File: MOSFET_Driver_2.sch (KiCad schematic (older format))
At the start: 20 parts, among them Q10 TPHR8504PL, Q11 TPHR8504PL, Q12 TPHR8504PL, Q7 TPHR8504PL, Q8 TPHR8504PL, Q9 TPHR8504PL, U1 FD6288Q

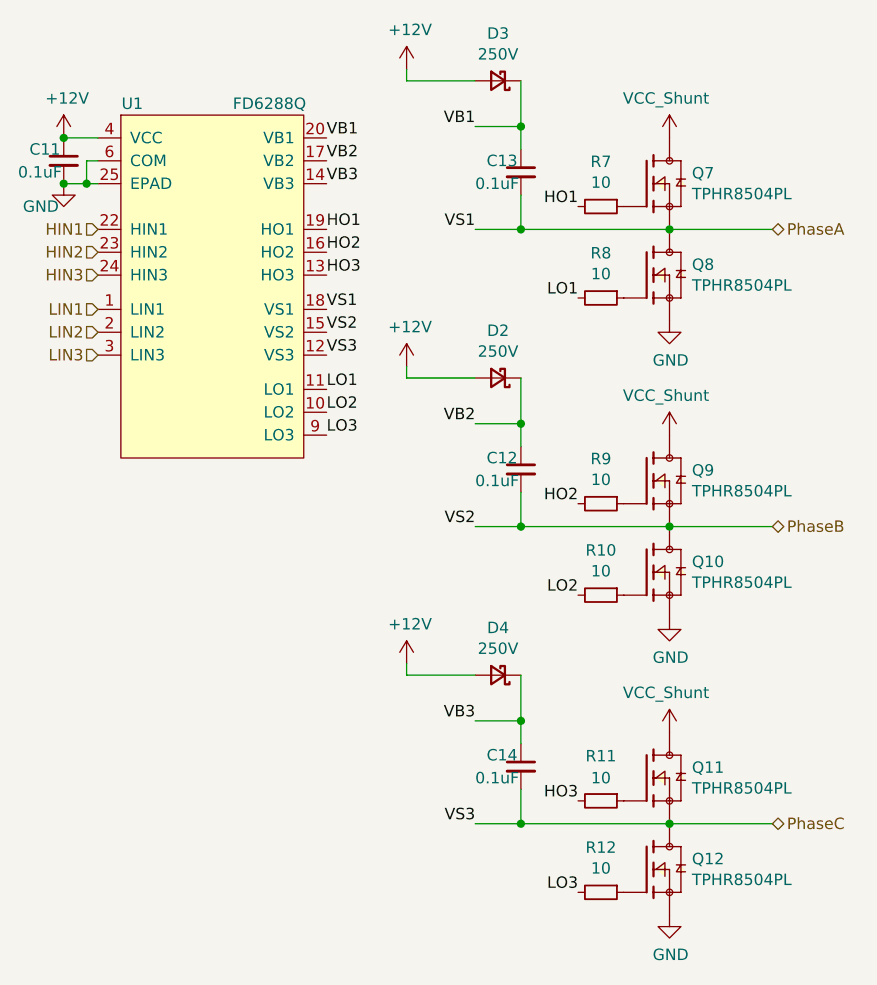
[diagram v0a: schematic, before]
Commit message: Added the rest of the phases and their associated components
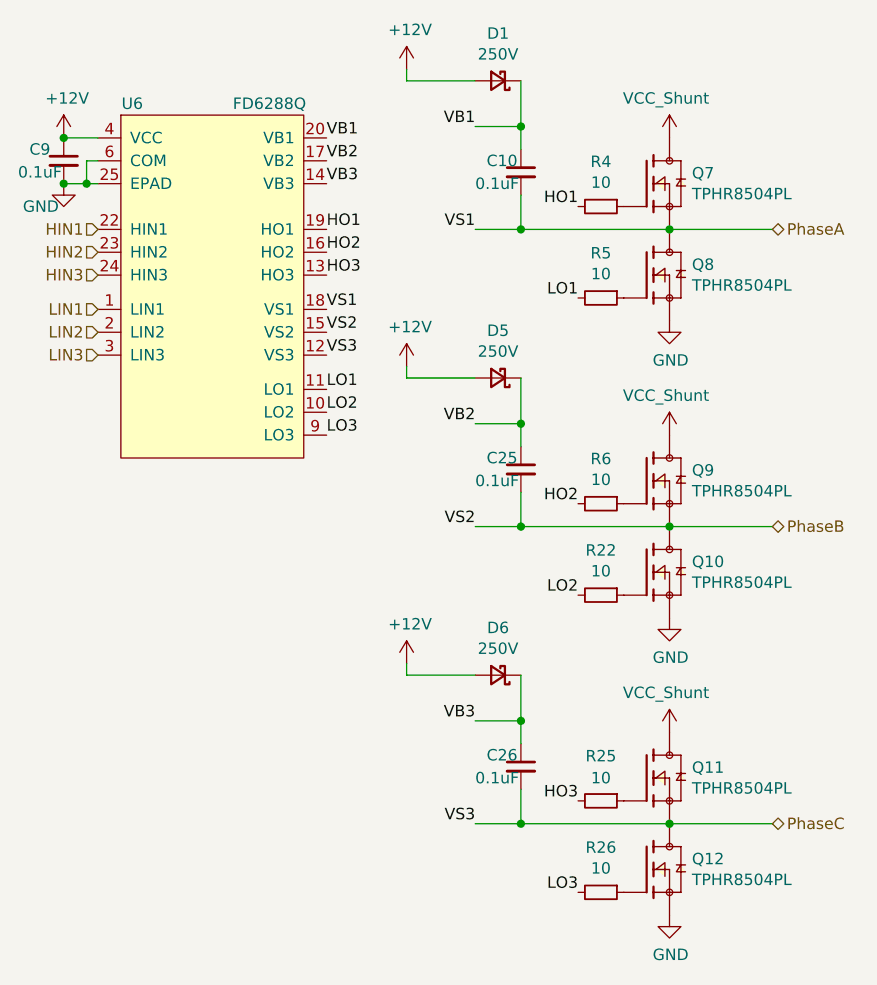
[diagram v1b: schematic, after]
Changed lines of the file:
@@
 $Descr A4 11693 8268
 encoding utf-8
-Sheet 6 7
+Sheet 7 11
 Title ""
 Date ""
@@
 AR Path="/605793F0/603754E4" Ref="U6"  Part="1"
 AR Path="/6057AB51/603754E4" Ref="U?"  Part="1"
-F 0 "U?" H 5800 1650 50  0000 C CNN
+F 0 "U6" H 5800 1650 50  0000 C CNN
 F 1 "FD6288Q" H 6400 1650 50  0000 C CNN
 F 2 "Package_DFN_QFN:QFN-24-1EP_4x4mm_P0.5mm_EP2.7x2.7mm" H 6175 2000 50  0001 C CNN
@@
 AR Path="/605793F0/6057ED5C" Ref="#PWR0136"  Part="1"
 AR Path="/6057AB51/6057ED5C" Ref="#PWR?"  Part="1"
-F 0 "#PWR?" H 5500 1950 50  0001 C CNN
+F 0 "#PWR0136" H 5500 1950 50  0001 C CNN
 F 1 "GND" H 5400 2100 50  0000 C CNN
 F 2 "" H 5500 2200 50  0001 C CNN
@@
 AR Path="/605793F0/6057ED5D" Ref="C9"  Part="1"
 AR Path="/6057AB51/6057ED5D" Ref="C?"  Part="1"
-F 0 "C?" H 5350 2150 50  0000 L CNN
+F 0 "C9" H 5350 2150 50  0000 L CNN
 F 1 "0.1uF" H 5300 2050 50  0000 L CNN
 F 2 "Capacitor_SMD:C_0402_1005Metric" H 5500 2100 50  0001 C CNN
@@
 AR Path="/605793F0/6057ED6E" Ref="#PWR0137"  Part="1"
 AR Path="/6057AB51/6057ED6E" Ref="#PWR?"  Part="1"
-F 0 "#PWR?" H 8150 2550 50  0001 C CNN
+F 0 "#PWR0137" H 8150 2550 50  0001 C CNN
 F 1 "GND" H 8155 2627 50  0000 C CNN
 F 2 "" H 8150 2800 50  0001 C CNN
@@
 AR Path="/605793F0/6057B9E1" Ref="R5"  Part="1"
 AR Path="/6057AB51/6057B9E1" Ref="R?"  Part="1"
-F 0 "R?" V 7654 2700 50  0000 C CNN
+F 0 "R5" V 7654 2700 50  0000 C CNN
 F 1 "10" V 7745 2700 50  0000 C CNN
 F 2 "Resistor_SMD:R_0402_1005Metric" H 7850 2700 50  0001 C CNN
@@
 AR Path="/605793F0/6057B9E2" Ref="R4"  Part="1"
 AR Path="/6057AB51/6057B9E2" Ref="R?"  Part="1"
-F 0 "R?" V 7654 2300 50  0000 C CNN
+F 0 "R4" V 7654 2300 50  0000 C CNN
 F 1 "10" V 7745 2300 50  0000 C CNN
 F 2 "Resistor_SMD:R_0402_1005Metric" H 7850 2300 50  0001 C CNN
@@
 AR Path="/605793F0/6057B9E3" Ref="#PWR0138"  Part="1"
 AR Path="/6057AB51/6057B9E3" Ref="#PWR?"  Part="1"
-F 0 "#PWR?" H 8150 3850 50  0001 C CNN
+F 0 "#PWR0138" H 8150 3850 50  0001 C CNN
 F 1 "GND" H 8155 3927 50  0000 C CNN
 F 2 "" H 8150 4100 50  0001 C CNN
@@
 AR Path="/605793F0/6057B9E4" Ref="R22"  Part="1"
 AR Path="/6057AB51/6057B9E4" Ref="R?"  Part="1"
-F 0 "R?" V 7654 4000 50  0000 C CNN
+F 0 "R22" V 7654 4000 50  0000 C CNN
 F 1 "10" V 7745 4000 50  0000 C CNN
 F 2 "Resistor_SMD:R_0402_1005Metric" H 7850 4000 50  0001 C CNN
@@
 AR Path="/605793F0/6057B9E5" Ref="R6"  Part="1"
 AR Path="/6057AB51/6057B9E5" Ref="R?"  Part="1"
-F 0 "R?" V 7654 3600 50  0000 C CNN
+F 0 "R6" V 7654 3600 50  0000 C CNN
 F 1 "10" V 7745 3600 50  0000 C CNN
 F 2 "Resistor_SMD:R_0402_1005Metric" H 7850 3600 50  0001 C CNN
@@
 AR Path="/605793F0/6057ED61" Ref="#PWR0139"  Part="1"
 AR Path="/6057AB51/6057ED61" Ref="#PWR?"  Part="1"
-F 0 "#PWR?" H 8150 5150 50  0001 C CNN
+F 0 "#PWR0139" H 8150 5150 50  0001 C CNN
 F 1 "GND" H 8155 5227 50  0000 C CNN
 F 2 "" H 8150 5400 50  0001 C CNN
@@
 AR Path="/605793F0/6057ED62" Ref="R26"  Part="1"
 AR Path="/6057AB51/6057ED62" Ref="R?"  Part="1"
-F 0 "R?" V 7654 5300 50  0000 C CNN
+F 0 "R26" V 7654 5300 50  0000 C CNN
 F 1 "10" V 7745 5300 50  0000 C CNN
 F 2 "Resistor_SMD:R_0402_1005Metric" H 7850 5300 50  0001 C CNN
@@
 AR Path="/605793F0/6057ED5E" Ref="D5"  Part="1"
 AR Path="/6057AB51/6057ED5E" Ref="D?"  Part="1"
-F 0 "D?" H 7400 2843 50  0000 C CNN
+F 0 "D5" H 7400 2843 50  0000 C CNN
 F 1 "250V" H 7400 2934 50  0000 C CNN
 F 2 "Diode_SMD:D_SOD-523" V 7400 3050 50  0001 C CNN
@@
 AR Path="/605793F0/6057ED5F" Ref="C25"  Part="1"
 AR Path="/6057AB51/6057ED5F" Ref="C?"  Part="1"
-F 0 "C?" H 7350 3500 50  0000 L CNN
+F 0 "C25" H 7350 3500 50  0000 L CNN
 F 1 "0.1uF" H 7300 3400 50  0000 L CNN
 F 2 "Capacitor_SMD:C_0603_1608Metric" H 7500 3450 50  0001 C CNN
@@
 AR Path="/605793F0/6057ED6F" Ref="D1"  Part="1"
 AR Path="/6057AB51/6057ED6F" Ref="D?"  Part="1"
-F 0 "D?" H 7400 1543 50  0000 C CNN
+F 0 "D1" H 7400 1543 50  0000 C CNN
 F 1 "250V" H 7400 1634 50  0000 C CNN
 F 2 "Diode_SMD:D_SOD-523" V 7400 1750 50  0001 C CNN
@@
 AR Path="/605793F0/6057ED60" Ref="C10"  Part="1"
 AR Path="/6057AB51/6057ED60" Ref="C?"  Part="1"
-F 0 "C?" H 7350 2200 50  0000 L CNN
+F 0 "C10" H 7350 2200 50  0000 L CNN
 F 1 "0.1uF" H 7300 2100 50  0000 L CNN
 F 2 "Capacitor_SMD:C_0603_1608Metric" H 7500 2150 50  0001 C CNN
@@
 AR Path="/605793F0/6057B9DF" Ref="D6"  Part="1"
 AR Path="/6057AB51/6057B9DF" Ref="D?"  Part="1"
-F 0 "D?" H 7400 4143 50  0000 C CNN
+F 0 "D6" H 7400 4143 50  0000 C CNN
 F 1 "250V" H 7400 4234 50  0000 C CNN
 F 2 "Diode_SMD:D_SOD-523" V 7400 4350 50  0001 C CNN
@@
 AR Path="/605793F0/6057ED71" Ref="C26"  Part="1"
 AR Path="/6057AB51/6057ED71" Ref="C?"  Part="1"
-F 0 "C?" H 7350 4800 50  0000 L CNN
+F 0 "C26" H 7350 4800 50  0000 L CNN
 F 1 "0.1uF" H 7300 4700 50  0000 L CNN
 F 2 "Capacitor_SMD:C_0603_1608Metric" H 7500 4750 50  0001 C CNN
@@
 AR Path="/605793F0/6057ED63" Ref="#PWR0140"  Part="1"
 AR Path="/6057AB51/6057ED63" Ref="#PWR?"  Part="1"
-F 0 "#PWR?" H 5500 1850 50  0001 C CNN
+F 0 "#PWR0140" H 5500 1850 50  0001 C CNN
 F 1 "+12V" H 5515 2173 50  0000 C CNN
 F 2 "" H 5500 2000 50  0001 C CNN
@@
 AR Path="/605793F0/6057ED78" Ref="#PWR0141"  Part="1"
 AR Path="/6057AB51/6057ED78" Ref="#PWR?"  Part="1"
-F 0 "#PWR?" H 7000 2850 50  0001 C CNN
+F 0 "#PWR0141" H 7000 2850 50  0001 C CNN
 F 1 "+12V" H 7015 3173 50  0000 C CNN
 F 2 "" H 7000 3000 50  0001 C CNN
@@
 AR Path="/605793F0/60380C9A" Ref="#PWR0142"  Part="1"
 AR Path="/6057AB51/60380C9A" Ref="#PWR?"  Part="1"
-F 0 "#PWR?" H 7000 1550 50  0001 C CNN
+F 0 "#PWR0142" H 7000 1550 50  0001 C CNN
 F 1 "+12V" H 7015 1873 50  0000 C CNN
 F 2 "" H 7000 1700 50  0001 C CNN
@@
 AR Path="/605793F0/6038180B" Ref="#PWR0143"  Part="1"
 AR Path="/6057AB51/6038180B" Ref="#PWR?"  Part="1"
-F 0 "#PWR?" H 7000 4150 50  0001 C CNN
+F 0 "#PWR0143" H 7000 4150 50  0001 C CNN
 F 1 "+12V" H 7015 4473 50  0000 C CNN
 F 2 "" H 7000 4300 50  0001 C CNN
@@
 AR Path="/605793F0/6057ED77" Ref="R25"  Part="1"
 AR Path="/6057AB51/6057ED77" Ref="R?"  Part="1"
-F 0 "R?" V 7654 4900 50  0000 C CNN
+F 0 "R25" V 7654 4900 50  0000 C CNN
 F 1 "10" V 7750 4900 50  0000 C CNN
 F 2 "Resistor_SMD:R_0402_1005Metric" H 7850 4900 50  0001 C CNN
@@
 AR Path="/605793F0/6057ED79" Ref="#PWR0144"  Part="1"
 AR Path="/6057AB51/6057ED79" Ref="#PWR?"  Part="1"
-F 0 "#PWR?" H 8150 1950 50  0001 C CNN
+F 0 "#PWR0144" H 8150 1950 50  0001 C CNN
 F 1 "VCC_Shunt" H 8135 2173 50  0000 C CNN
 F 2 "" H 8150 2000 50  0001 C CNN
@@
 AR Path="/605793F0/60480DE3" Ref="#PWR0145"  Part="1"
 AR Path="/6057AB51/60480DE3" Ref="#PWR?"  Part="1"
-F 0 "#PWR?" H 8150 3250 50  0001 C CNN
+F 0 "#PWR0145" H 8150 3250 50  0001 C CNN
 F 1 "VCC_Shunt" H 8135 3473 50  0000 C CNN
 F 2 "" H 8150 3300 50  0001 C CNN
@@
 AR Path="/605793F0/6057ED7A" Ref="#PWR0146"  Part="1"
 AR Path="/6057AB51/6057ED7A" Ref="#PWR?"  Part="1"
-F 0 "#PWR?" H 8150 4550 50  0001 C CNN
+F 0 "#PWR0146" H 8150 4550 50  0001 C CNN
 F 1 "VCC_Shunt" H 8135 4773 50  0000 C CNN
 F 2 "" H 8150 4600 50  0001 C CNN
@@
 AR Path="/605793F0/6051C969" Ref="Q7"  Part="1"
 AR Path="/6057AB51/6051C969" Ref="Q?"  Part="1"
-F 0 "Q?" H 8248 2246 50  0000 L CNN
+F 0 "Q7" H 8248 2246 50  0000 L CNN
 F 1 "TPHR8504PL" H 8248 2155 50  0000 L CNN
 F 2 "Footprints:TPHR8504PL" H 8300 2450 50  0001 L BNN
@@
 AR Path="/605793F0/6051E952" Ref="Q8"  Part="1"
 AR Path="/6057AB51/6051E952" Ref="Q?"  Part="1"
-F 0 "Q?" H 8248 2646 50  0000 L CNN
+F 0 "Q8" H 8248 2646 50  0000 L CNN
 F 1 "TPHR8504PL" H 8248 2555 50  0000 L CNN
 F 2 "Footprints:TPHR8504PL" H 8300 2850 50  0001 L BNN
@@
 AR Path="/605793F0/6057ED68" Ref="Q9"  Part="1"
 AR Path="/6057AB51/6057ED68" Ref="Q?"  Part="1"
-F 0 "Q?" H 8248 3546 50  0000 L CNN
+F 0 "Q9" H 8248 3546 50  0000 L CNN
 F 1 "TPHR8504PL" H 8248 3455 50  0000 L CNN
 F 2 "Footprints:TPHR8504PL" H 8300 3750 50  0001 L BNN
@@
 AR Path="/605793F0/6057ED69" Ref="Q10"  Part="1"
 AR Path="/6057AB51/6057ED69" Ref="Q?"  Part="1"
-F 0 "Q?" H 8248 3946 50  0000 L CNN
+F 0 "Q10" H 8248 3946 50  0000 L CNN
 F 1 "TPHR8504PL" H 8248 3855 50  0000 L CNN
 F 2 "Footprints:TPHR8504PL" H 8300 4150 50  0001 L BNN
@@
 AR Path="/605793F0/6057ED6A" Ref="Q11"  Part="1"
 AR Path="/6057AB51/6057ED6A" Ref="Q?"  Part="1"
-F 0 "Q?" H 8248 4846 50  0000 L CNN
+F 0 "Q11" H 8248 4846 50  0000 L CNN
 F 1 "TPHR8504PL" H 8248 4755 50  0000 L CNN
 F 2 "Footprints:TPHR8504PL" H 8300 5050 50  0001 L BNN
@@
 AR Path="/605793F0/6051B473" Ref="Q12"  Part="1"
 AR Path="/6057AB51/6051B473" Ref="Q?"  Part="1"
-F 0 "Q?" H 8248 5246 50  0000 L CNN
+F 0 "Q12" H 8248 5246 50  0000 L CNN
 F 1 "TPHR8504PL" H 8248 5155 50  0000 L CNN
 F 2 "Footprints:TPHR8504PL" H 8300 5450 50  0001 L BNN

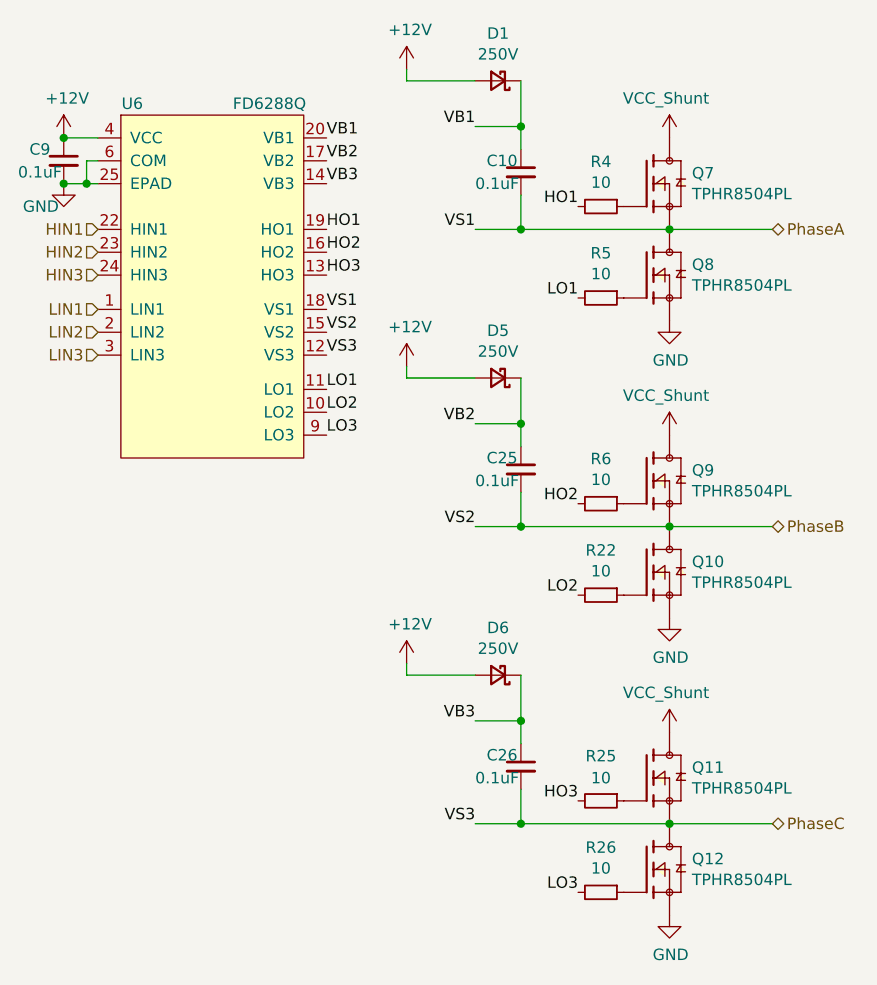
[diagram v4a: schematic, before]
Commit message: Finished all traces and vias
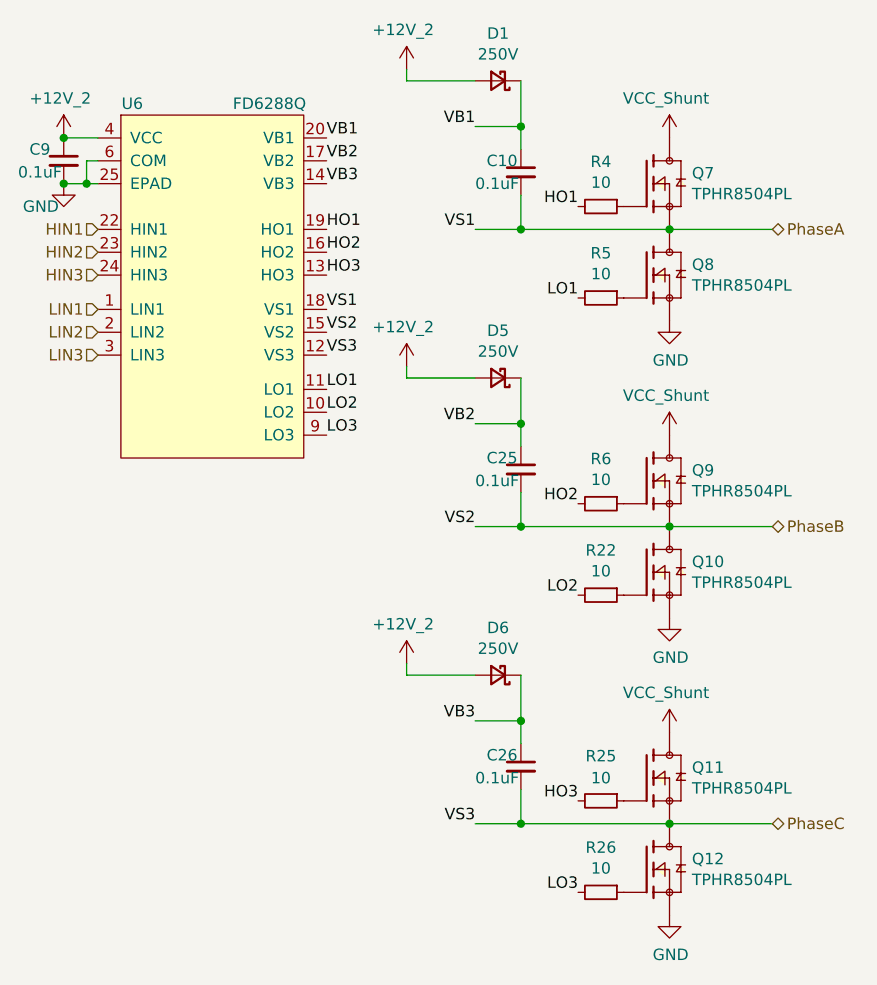
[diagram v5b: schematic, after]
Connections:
- net +12V renamed +12V_2
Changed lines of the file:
@@
 	7500 4850 7500 5000
 Connection ~ 7500 5000
-$Comp
-L power:+12V #PWR02
-U 1 1 6057ED63
-P 5500 2000
-AR Path="/6035042B/6057ED63" Ref="#PWR02"  Part="1"
-AR Path="/605793F0/6057ED63" Ref="#PWR0140"  Part="1"
-AR Path="/6057AB51/6057ED63" Ref="#PWR?"  Part="1"
-AR Path="/6054D33A/6057ED63" Ref="#PWR0169"  Part="1"
-AR Path="/60568CDE/6057ED63" Ref="#PWR?"  Part="1"
-AR Path="/6057505F/6057ED63" Ref="#PWR?"  Part="1"
-AR Path="/60595220/6057ED63" Ref="#PWR0198"  Part="1"
-AR Path="/605A2EC4/6057ED63" Ref="#PWR0227"  Part="1"
-AR Path="/60536007/6057ED63" Ref="#PWR0196"  Part="1"
-F 0 "#PWR0140" H 5500 1850 50  0001 C CNN
-F 1 "+12V" H 5515 2173 50  0000 C CNN
-F 2 "" H 5500 2000 50  0001 C CNN
-F 3 "" H 5500 2000 50  0001 C CNN
-	1    5500 2000
-	1    0    0    -1
-$EndComp
-$Comp
-L power:+12V #PWR03
-U 1 1 6057ED78
-P 7000 3000
-AR Path="/6035042B/6057ED78" Ref="#PWR03"  Part="1"
-AR Path="/605793F0/6057ED78" Ref="#PWR0141"  Part="1"
-AR Path="/6057AB51/6057ED78" Ref="#PWR?"  Part="1"
-AR Path="/6054D33A/6057ED78" Ref="#PWR0170"  Part="1"
-AR Path="/60568CDE/6057ED78" Ref="#PWR?"  Part="1"
-AR Path="/6057505F/6057ED78" Ref="#PWR?"  Part="1"
-AR Path="/60595220/6057ED78" Ref="#PWR0199"  Part="1"
-AR Path="/605A2EC4/6057ED78" Ref="#PWR0228"  Part="1"
-AR Path="/60536007/6057ED78" Ref="#PWR0197"  Part="1"
-F 0 "#PWR0141" H 7000 2850 50  0001 C CNN
-F 1 "+12V" H 7015 3173 50  0000 C CNN
-F 2 "" H 7000 3000 50  0001 C CNN
-F 3 "" H 7000 3000 50  0001 C CNN
-	1    7000 3000
-	1    0    0    -1
-$EndComp
-$Comp
-L power:+12V #PWR01
-U 1 1 60380C9A
-P 7000 1700
-AR Path="/6035042B/60380C9A" Ref="#PWR01"  Part="1"
-AR Path="/605793F0/60380C9A" Ref="#PWR0142"  Part="1"
-AR Path="/6057AB51/60380C9A" Ref="#PWR?"  Part="1"
-AR Path="/6054D33A/60380C9A" Ref="#PWR0171"  Part="1"
-AR Path="/60568CDE/60380C9A" Ref="#PWR?"  Part="1"
-AR Path="/6057505F/60380C9A" Ref="#PWR?"  Part="1"
-AR Path="/60595220/60380C9A" Ref="#PWR0200"  Part="1"
-AR Path="/605A2EC4/60380C9A" Ref="#PWR0229"  Part="1"
-AR Path="/60536007/60380C9A" Ref="#PWR0198"  Part="1"
-F 0 "#PWR0142" H 7000 1550 50  0001 C CNN
-F 1 "+12V" H 7015 1873 50  0000 C CNN
-F 2 "" H 7000 1700 50  0001 C CNN
-F 3 "" H 7000 1700 50  0001 C CNN
-	1    7000 1700
-	1    0    0    -1
-$EndComp
-$Comp
-L power:+12V #PWR04
-U 1 1 6038180B
-P 7000 4300
-AR Path="/6035042B/6038180B" Ref="#PWR04"  Part="1"
-AR Path="/605793F0/6038180B" Ref="#PWR0143"  Part="1"
-AR Path="/6057AB51/6038180B" Ref="#PWR?"  Part="1"
-AR Path="/6054D33A/6038180B" Ref="#PWR0172"  Part="1"
-AR Path="/60568CDE/6038180B" Ref="#PWR?"  Part="1"
-AR Path="/6057505F/6038180B" Ref="#PWR?"  Part="1"
-AR Path="/60595220/6038180B" Ref="#PWR0201"  Part="1"
-AR Path="/605A2EC4/6038180B" Ref="#PWR0230"  Part="1"
-AR Path="/60536007/6038180B" Ref="#PWR0199"  Part="1"
-F 0 "#PWR0143" H 7000 4150 50  0001 C CNN
-F 1 "+12V" H 7015 4473 50  0000 C CNN
-F 2 "" H 7000 4300 50  0001 C CNN
-F 3 "" H 7000 4300 50  0001 C CNN
-	1    7000 4300
-	1    0    0    -1
-$EndComp
 $Bitmap
 Pos 4150 2500
@@
 Wire Wire Line
 	5500 2000 5650 2000
-Connection ~ 5500 2000
 Wire Wire Line
 	5650 2200 5600 2200
@@
 	1    0    0    -1
 $EndComp
+$Comp
+L power:+12V_2 #PWR0140
+U 1 1 606F346B
+P 5500 2000
+F 0 "#PWR0140" H 5500 1950 50  0001 C CNN
+F 1 "+12V_2" H 5485 2173 50  0000 C CNN
+F 2 "" H 5500 2000 50  0001 C CNN
+F 3 "" H 5500 2000 50  0001 C CNN
+	1    5500 2000
+	1    0    0    -1
+$EndComp
+Connection ~ 5500 2000
+$Comp
+L power:+12V_2 #PWR0141
+U 1 1 606F3C82
+P 7000 1700
+F 0 "#PWR0141" H 7000 1650 50  0001 C CNN
+F 1 "+12V_2" H 6985 1873 50  0000 C CNN
+F 2 "" H 7000 1700 50  0001 C CNN
+F 3 "" H 7000 1700 50  0001 C CNN
+	1    7000 1700
+	1    0    0    -1
+$EndComp
+$Comp
+L power:+12V_2 #PWR0142
+U 1 1 606F4024
+P 7000 3000
+F 0 "#PWR0142" H 7000 2950 50  0001 C CNN
+F 1 "+12V_2" H 6985 3173 50  0000 C CNN
+F 2 "" H 7000 3000 50  0001 C CNN
+F 3 "" H 7000 3000 50  0001 C CNN
+	1    7000 3000
+	1    0    0    -1
+$EndComp
+$Comp
+L power:+12V_2 #PWR0143
+U 1 1 606F4498
+P 7000 4300
+F 0 "#PWR0143" H 7000 4250 50  0001 C CNN
+F 1 "+12V_2" H 6985 4473 50  0000 C CNN
+F 2 "" H 7000 4300 50  0001 C CNN
+F 3 "" H 7000 4300 50  0001 C CNN
+	1    7000 4300
+	1    0    0    -1
+$EndComp
